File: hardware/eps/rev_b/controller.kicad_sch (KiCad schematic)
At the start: 14 parts, among them J100 SWD_ACCESS_LOGICAL, U100 STM32G0B1KET6N, Y100 ECS-3225MV-160-BN-TR

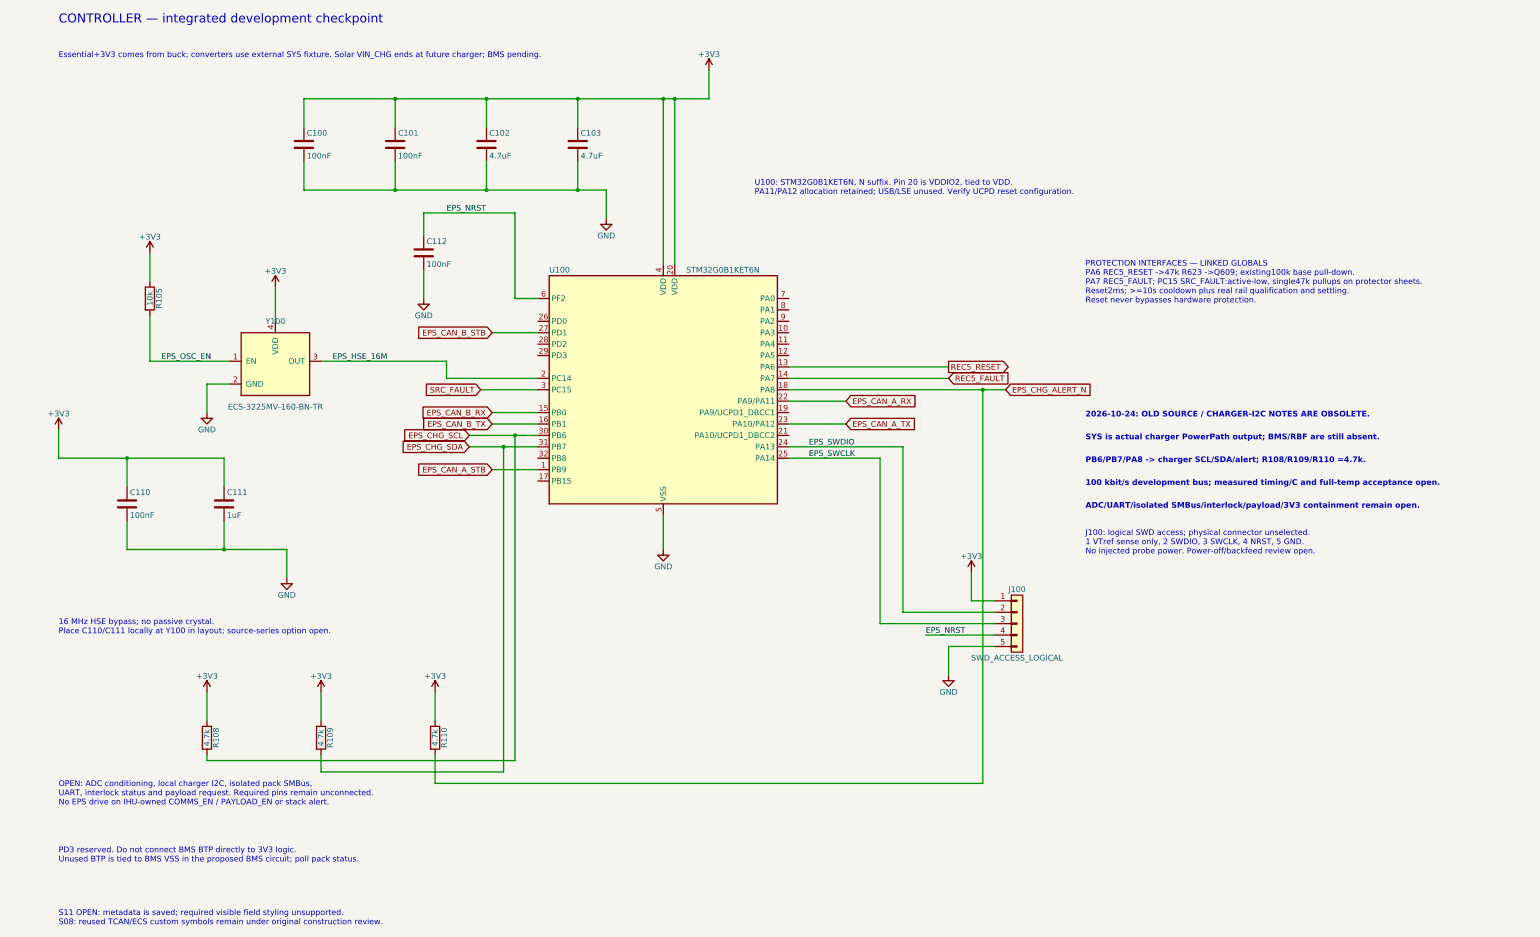
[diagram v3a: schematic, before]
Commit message: Integrate EPS Rev B battery management development circuit
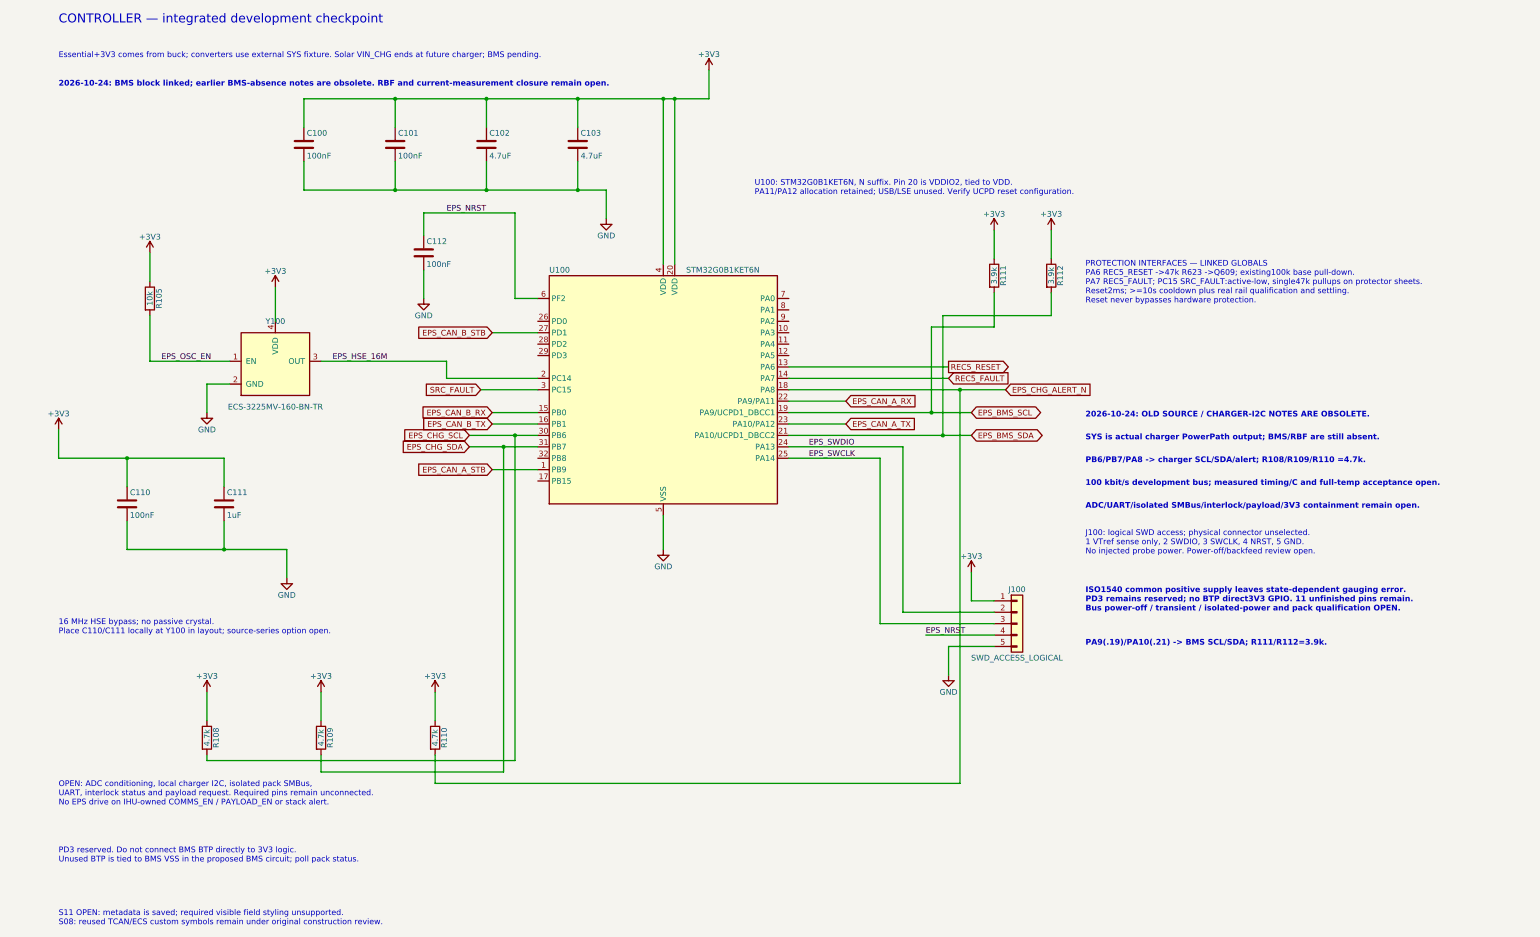
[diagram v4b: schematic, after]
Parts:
- added R111, R112: 3.9k, Resistor_SMD:R_0603_1608Metric, symbol Device:R
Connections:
- net +3V3: now also R111.1, R112.1
- net EPS_BMS_SCL: now reaches U100.19 (PA9/UCPD1_DBCC1)
- net EPS_BMS_SCL: now also R111.2
- net EPS_BMS_SDA: now reaches U100.21 (PA10/UCPD1_DBCC2)
- net EPS_BMS_SDA: now also R112.2
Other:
- note added: "2026-10-24: BMS block linked; earlier BMS-absence notes are obsolete. RBF and current-measurement closure remain open."
- note added: "ISO1540 common positive supply leaves state-dependent gauging error. PD3 remains reserved; no BTP direct3V3 GPIO. 11 unfinished pins remain. Bus power-off / transient / isolated-power and pack qualification OPEN."
- note added: "PA9(.19)/PA10(.21) -> BMS SCL/SDA; R111/R112=3.9k."

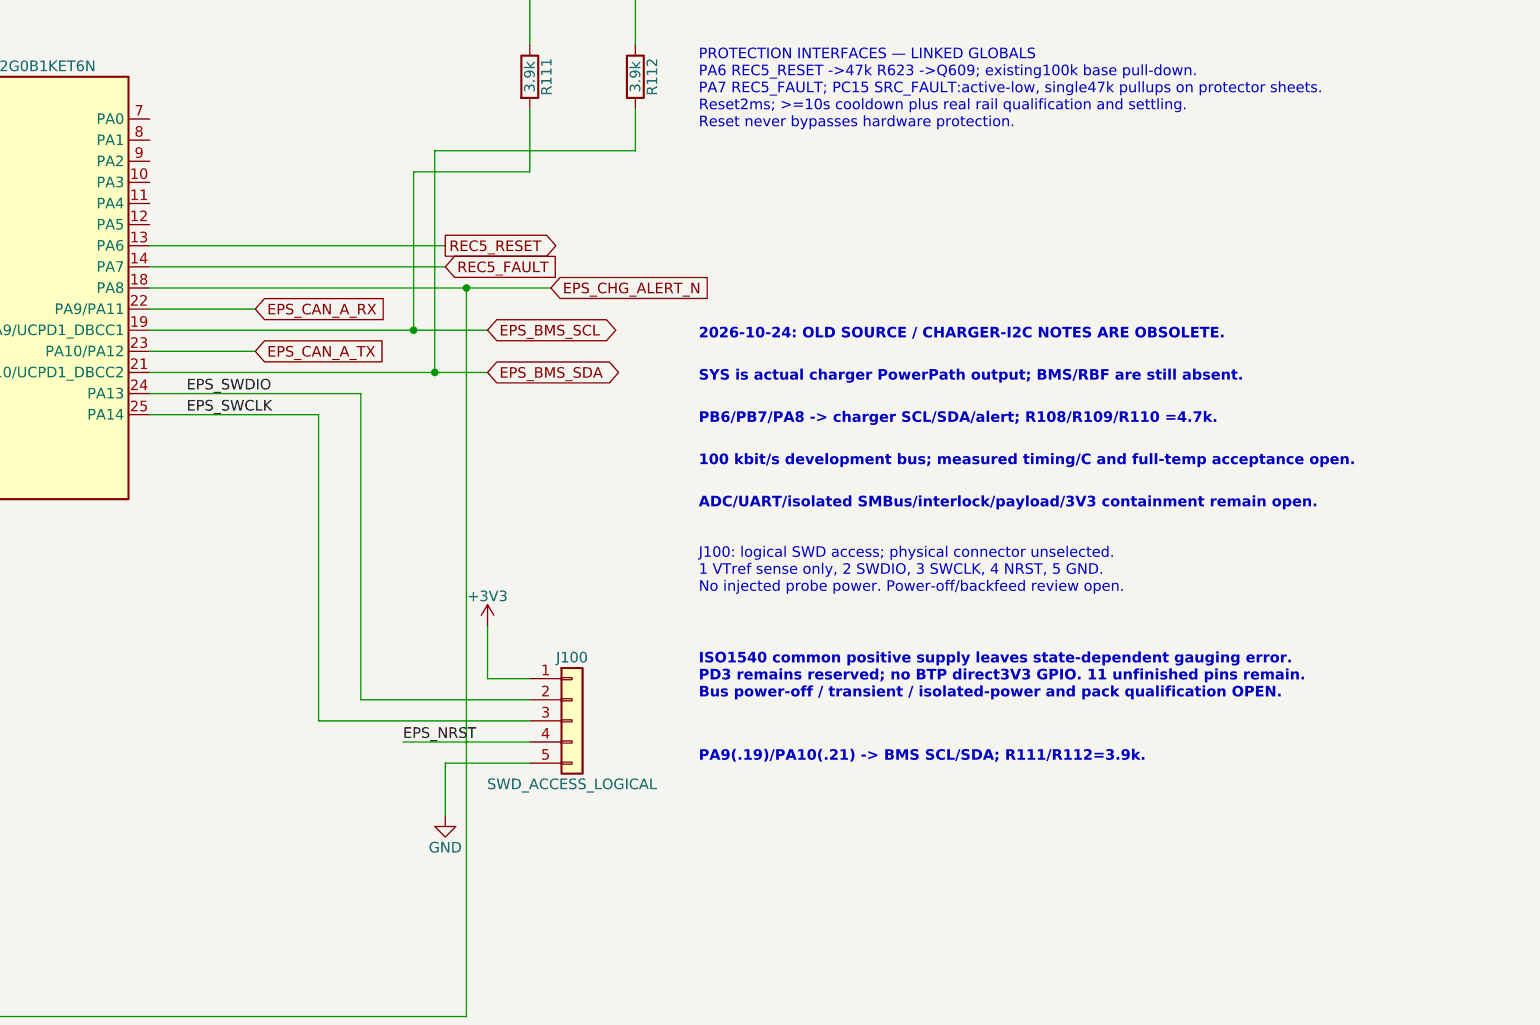
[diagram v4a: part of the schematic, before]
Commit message: Integrate buffered EPS UART debug interface
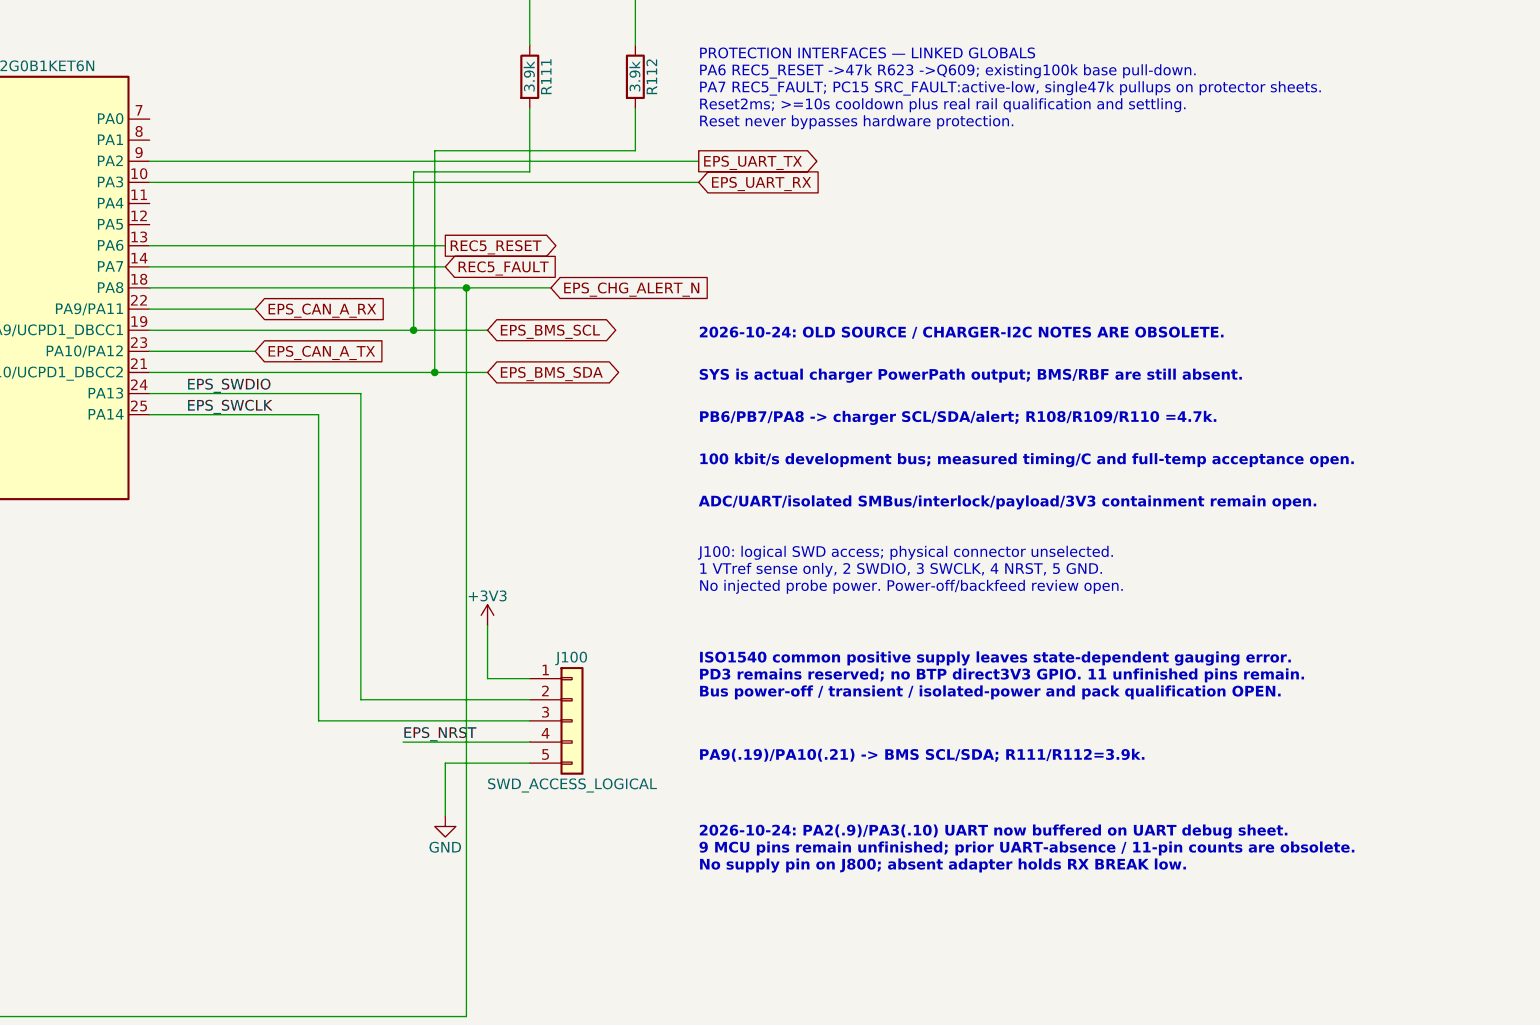
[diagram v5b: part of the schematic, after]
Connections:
- net EPS_UART_RX: now reaches U100.10 (PA3)
- net EPS_UART_TX: now reaches U100.9 (PA2)
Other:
- note added: "2026-10-24: PA2(.9)/PA3(.10) UART now buffered on UART debug sheet. 9 MCU pins remain unfinished; prior UART-absence / 11-pin counts are obsolete. No supply pin on J800; absent adapter holds RX BREAK low."
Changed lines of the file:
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@@
+		)
+	)
+	(wire
+		(pts
+			(xy 187.96 90.17)
+			(xy 254 90.17)
+		)
+	)
+	(wire
+		(pts
+			(xy 187.96 92.71)
+			(xy 254 92.71)
 		)
 	)
@@
 		)
 	)
+	(global_label "EPS_UART_TX"
+		(shape output)
+		(at 254 90.17 0)
+		(effects
+			(font
+				(size 1.27 1.27)
+			)
+			(justify left)
+		)
+	)
+	(global_label "EPS_UART_RX"
+		(shape input)
+		(at 254 92.71 0)
+		(effects
+			(font
+				(size 1.27 1.27)
+			)
+			(justify left)
+		)
+	)
+  (text "2026-10-24: PA2(.9)/PA3(.10) UART now buffered on UART debug sheet.\n9 MCU pins remain unfinished; prior UART-absence / 11-pin counts are obsolete.\nNo supply pin on J800; absent adapter holds RX BREAK low."
+    (at 254 170.18 0)
+    (effects (font (size 1.27 1.27) (bold yes)) (justify left top))
+  )
 	(symbol
 		(lib_id "Ember_EPS_Candidates:ECS_3225MV_DRAFT_v2")
